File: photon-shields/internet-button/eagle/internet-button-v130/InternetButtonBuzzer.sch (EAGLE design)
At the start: 39 parts

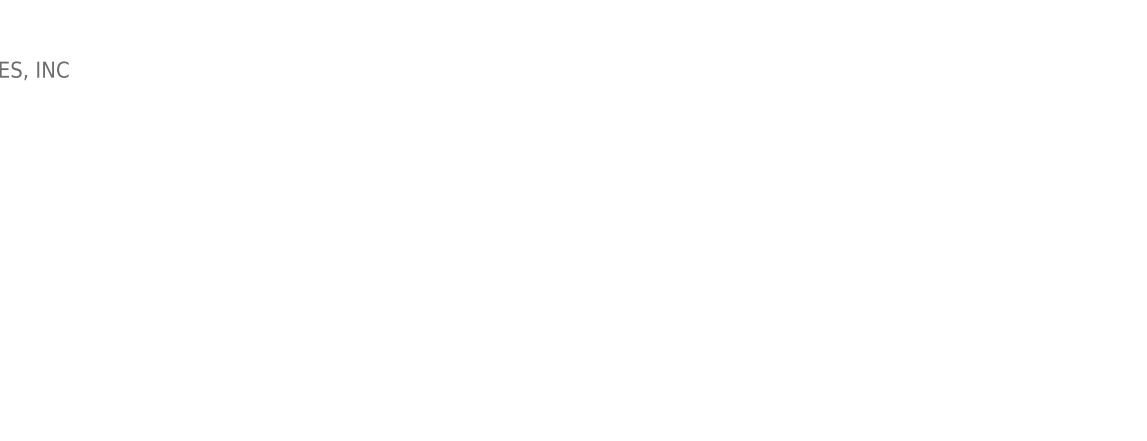
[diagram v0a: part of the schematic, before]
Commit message: added rev numbers to schematic sheets and regenerated the PDFs
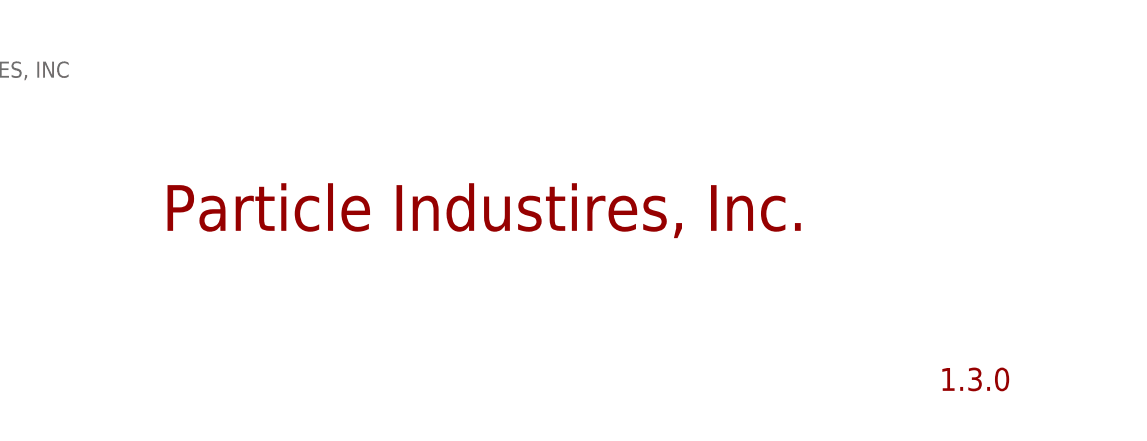
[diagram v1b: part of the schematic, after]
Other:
- note added: "1.3.0"
- note added: "Particle Industires, Inc."
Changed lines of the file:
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@@
 with this information.
 Particle is a registered trademark.</text>
+<text x="375.92" y="7.62" size="2.54" layer="94">1.3.0</text>
+<text x="289.56" y="25.4" size="5.08" layer="94">Particle Industires, Inc.</text>
 </plain>
 <instances>
